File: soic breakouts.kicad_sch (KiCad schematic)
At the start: 8 parts, among them J1 Conn_01x07, J2 Conn_01x07, J3 Conn_01x01, J4 Conn_01x08, J5 Conn_01x08, J6 Conn_01x01, U1 TL074, U2 LM13700

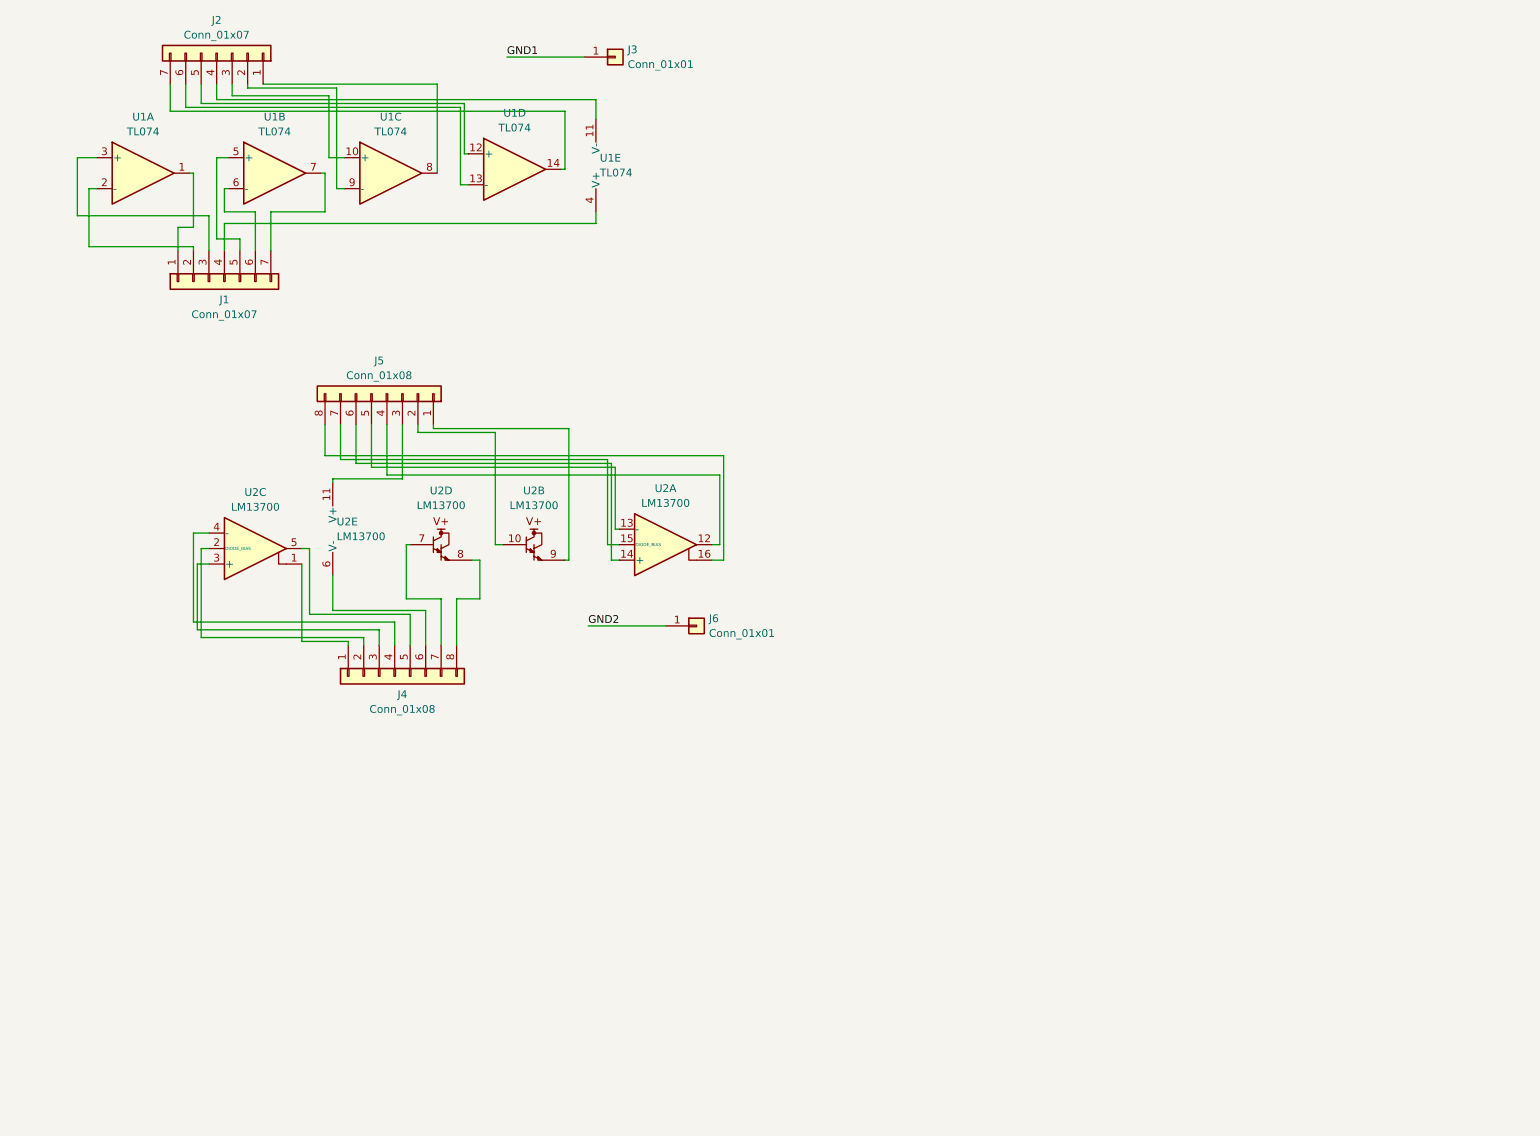
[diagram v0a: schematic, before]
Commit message: Add SOIC-8.
* Update to KiCAD 8 format.
* Add SOIC-8 footprint breakout.
* Update to new IPC pin 1 (triangle/arrow) indicator throughout.
* Make pin 1 on header more obvious with IPC indicator throughout.
* Increase silkscreen font size for main label per breakout board.
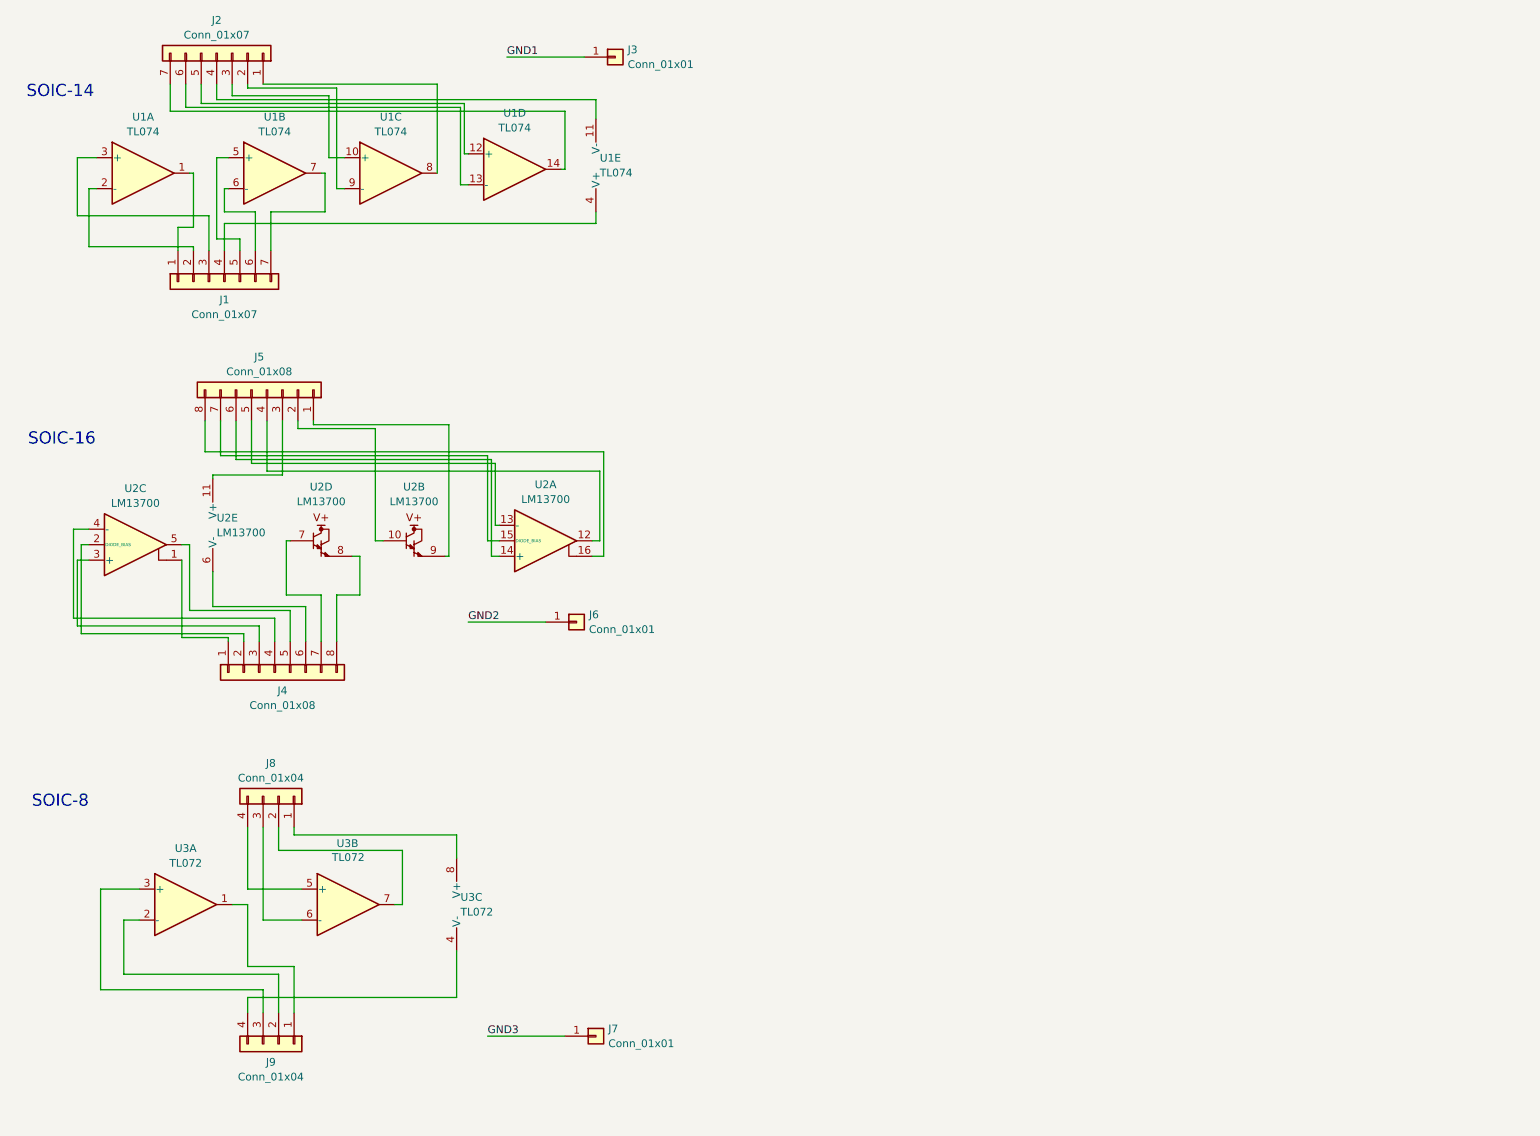
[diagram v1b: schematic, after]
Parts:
- added J7: Conn_01x01, Aaron_Pads:TP_HeaderPin_P2.54mm_round, symbol Connector_Generic:Conn_01x01
- added J8, J9: Conn_01x04, Connector_PinHeader_2.54mm:PinHeader_1x04_P2.54mm_Vertical, symbol Connector_Generic:Conn_01x04
- added U3: TL072, Aaron_TI_Parts:TI_SOIC_D_R-PDSO-8, symbol Amplifier_Operational:TL072
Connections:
- new net: J8.1 (Pin_1), U3.8 (V+)
- new net: J8.2 (Pin_2), U3.7
- new net: J8.3 (Pin_3), U3.6 (-)
- new net: J8.4 (Pin_4), U3.5 (+)
- new net: J9.1 (Pin_1), U3.1
- new net: J9.2 (Pin_2), U3.2 (-)
- new net: J9.3 (Pin_3), U3.3 (+)
- new net: J9.4 (Pin_4), U3.4 (V-)
- new net GND3: J7.1 (Pin_1)
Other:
- note added: "SOIC-14"
- note added: "SOIC-16"
- note added: "SOIC-8"
- moved on the sheet: J4, J5, J6, U2A, U2B, U2C, U2D, U2E

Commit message: Add TSSOP-8, -14, -16 breakouts.
Now have SOIC and TSSOP for 8/14/16 pin variants.
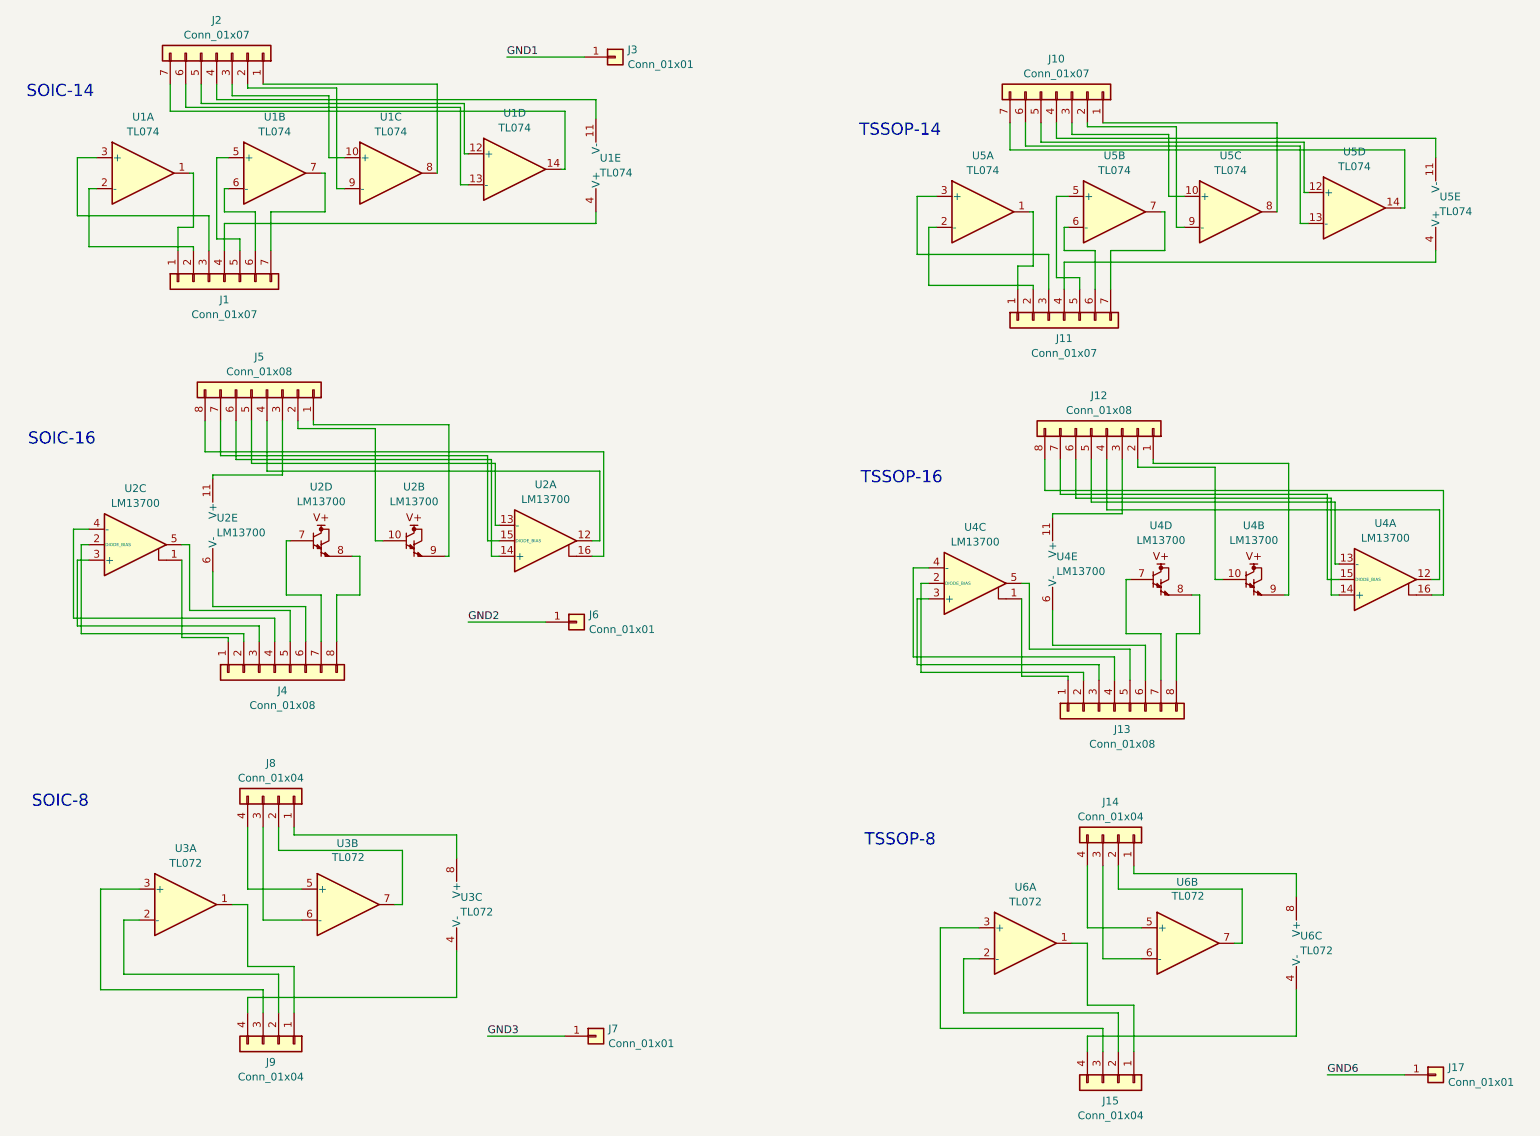
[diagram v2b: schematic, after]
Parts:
- added J10, J11: Conn_01x07, Connector_PinHeader_2.54mm:PinHeader_1x07_P2.54mm_Vertical, symbol Connector_Generic:Conn_01x07
- added J12, J13: Conn_01x08, Connector_PinHeader_2.54mm:PinHeader_1x08_P2.54mm_Vertical, symbol Connector_Generic:Conn_01x08
- added J14, J15: Conn_01x04, Connector_PinHeader_2.54mm:PinHeader_1x04_P2.54mm_Vertical, symbol Connector_Generic:Conn_01x04
- added J17: Conn_01x01, Aaron_Pads:TP_HeaderPin_P2.54mm_round, symbol Connector_Generic:Conn_01x01
- added U4: LM13700, Package_SO:TSSOP-16_4.4x5mm_P0.65mm, symbol Amplifier_Operational:LM13700
- added U5: TL074, Aaron_TI_Parts:TI_TSSOP_PW0014A, symbol Amplifier_Operational:TL074
- added U6: TL072, Aaron_TI_Parts:TI_TSSOP_PW0008A, symbol Amplifier_Operational:TL072
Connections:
- new net: J10.3 (Pin_3), U5.10 (+)
- new net: J10.1 (Pin_1), U5.8
- new net: J10.2 (Pin_2), U5.9 (-)
- new net: J11.1 (Pin_1), U5.1
- new net: J11.2 (Pin_2), U5.2 (-)
- new net: J11.3 (Pin_3), U5.3 (+)
- new net: J12.3 (Pin_3), U4.11 (V+)
- new net: J13.6 (Pin_6), U4.6 (V-)
- new net: J13.1 (Pin_1), U4.1
- new net: J13.2 (Pin_2), U4.2 (DIODE_BIAS)
- new net: J13.3 (Pin_3), U4.3 (+)
- new net: J13.4 (Pin_4), U4.4 (-)
- new net: J13.5 (Pin_5), U4.5
- new net: J12.1 (Pin_1), U4.9
- new net: J12.2 (Pin_2), U4.10
- new net: J12.4 (Pin_4), U4.12
- new net: J12.5 (Pin_5), U4.13 (-)
- new net: J12.6 (Pin_6), U4.14 (+)
- new net: J12.7 (Pin_7), U4.15 (DIODE_BIAS)
- new net: J12.8 (Pin_8), U4.16
- new net: J14.1 (Pin_1), U6.8 (V+)
- new net: J14.2 (Pin_2), U6.7
- new net: J14.3 (Pin_3), U6.6 (-)
- new net: J14.4 (Pin_4), U6.5 (+)
- new net: J15.1 (Pin_1), U6.1
- new net: J15.2 (Pin_2), U6.2 (-)
- new net: J15.3 (Pin_3), U6.3 (+)
- new net: J10.4 (Pin_4), U5.11 (V-)
- new net: J10.5 (Pin_5), U5.12 (+)
- new net: J10.6 (Pin_6), U5.13 (-)
- new net: J10.7 (Pin_7), U5.14
- new net: J15.4 (Pin_4), U6.4 (V-)
- new net: J11.5 (Pin_5), U5.5 (+)
- new net: J11.6 (Pin_6), U5.6 (-)
- new net: J11.7 (Pin_7), U5.7
- new net: J13.7 (Pin_7), U4.7
- new net: J13.8 (Pin_8), U4.8
- new net: J11.4 (Pin_4), U5.4 (V+)
- new net GND6: J17.1 (Pin_1)
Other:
- note added: "TSSOP-14"
- note added: "TSSOP-16"
- note added: "TSSOP-8"
